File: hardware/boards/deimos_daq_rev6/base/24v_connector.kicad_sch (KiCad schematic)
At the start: 16 parts, among them IC8001 INA826AIDR, J8001 Barrel_Jack PJ-202BH, U4001 INA181A2

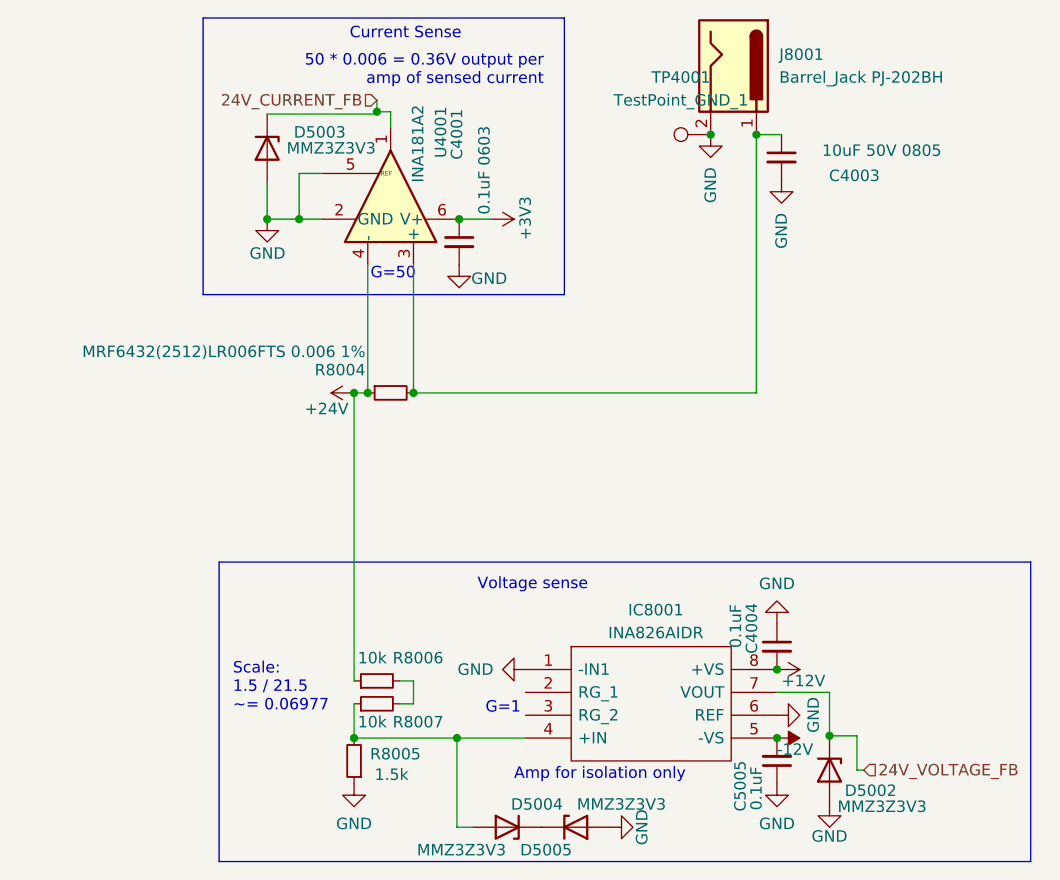
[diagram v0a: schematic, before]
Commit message: start updating layout. remove some unnecessary diodes from base module.
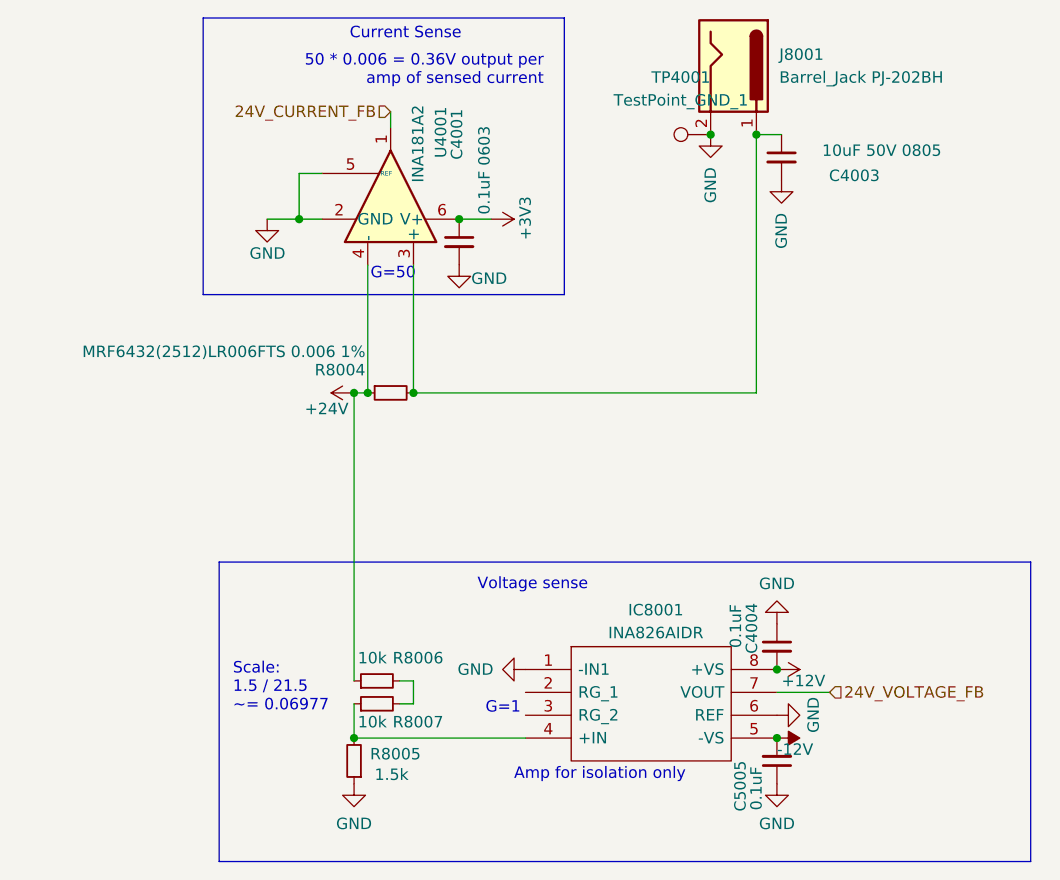
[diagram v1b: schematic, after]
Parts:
- removed D5002, D5003, D5004, D5005: MMZ3Z3V3, Diode_SMD:D_SOD-323, symbol Device:D_Zener
